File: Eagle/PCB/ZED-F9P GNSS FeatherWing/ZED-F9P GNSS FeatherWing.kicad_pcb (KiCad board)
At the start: 2 copper layers, 50.8 x 22.9 mm, 42 parts, among them Q1 DMG2305, U1 ZED-F9P_ZED-F9P, U2 SPX3819-3.3, X1 SMA-142-0711-821/826

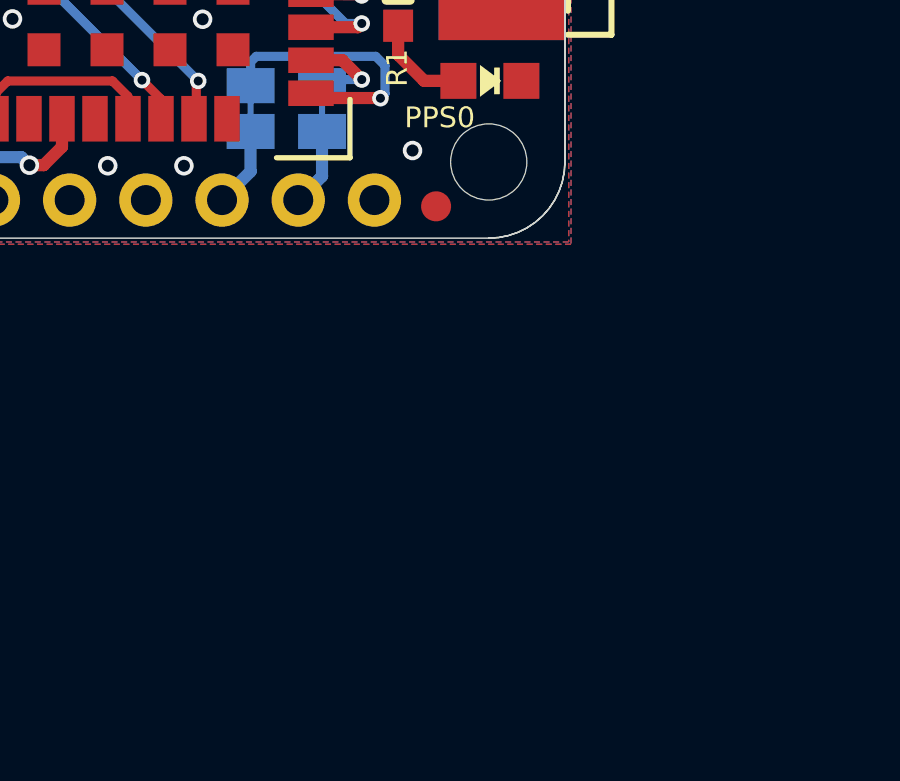
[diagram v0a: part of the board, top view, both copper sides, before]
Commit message: Update to Kicad 10 and added SMA
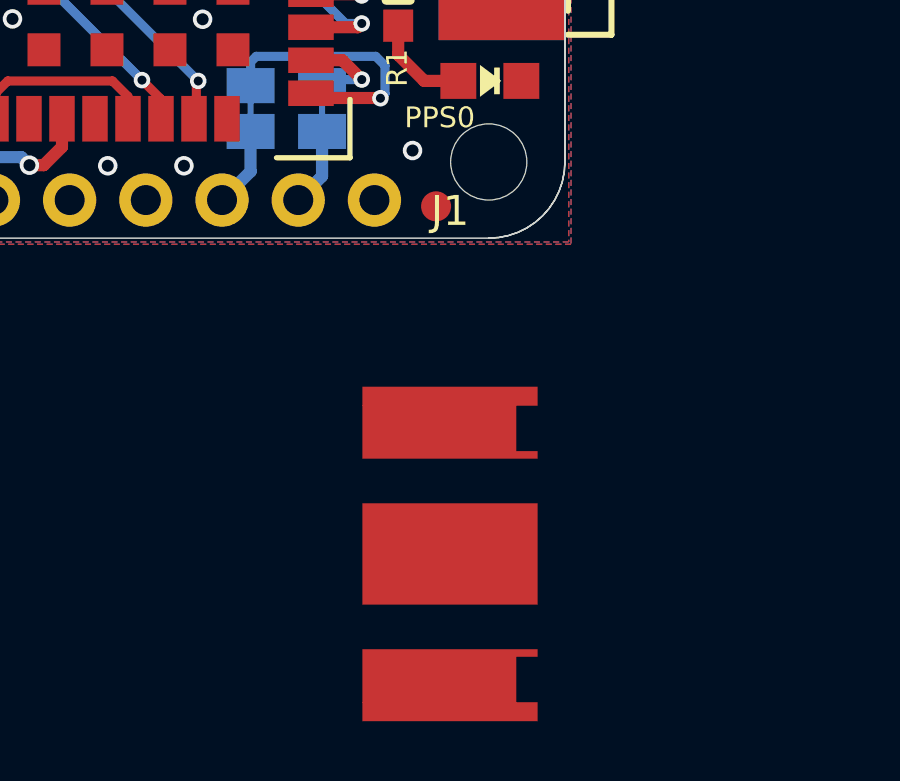
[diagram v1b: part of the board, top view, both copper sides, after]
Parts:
- added J1: Coupler_v2_Coupler_v2-rescue_SMA-Coupler_v1-rescue, Coupler_v1:SMA_Molex_732511150_v3, F.Cu at (170.1, 127.0)
- CON1: value (none) -> MICROBUILDER_USBFCI_10103594_CORRECTED
- CTS0, GND0, RTS0, RX2, TX2, UNK3V3: value (none) -> PINHD-1X1
- INT0, RX0, SCL0, SDA0, TX0: value (none) -> SOLDERJUMPERCLOSED
- JP5: value (none) -> HEADER-1X2ROUND
- TP1: value (none) -> TESTPOINTROUND1.5MM
- UNK3.3V0: value (none) -> SOLDERJUMPER
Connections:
- net 3V renamed Net-(MS1-3V)
- net ANT renamed /ANT
- net D+ renamed /D+
- net D- renamed /D-
- net EN renamed /EN
- net EXTINT renamed /EXTINT
- net RX renamed /RX
- net RX2 renamed /RX2
- net SAFEBOOT renamed /SAFEBOOT
- net SCL renamed /SCL
- net SDA renamed /SDA
- net TP renamed /TP
- net TX renamed /TX
- net TX2 renamed /TX2
- net VBACKUP renamed /VBACKUP
- net VCC_RF renamed /VCC_RF
- net ~{RESET} renamed /~{RESET}
- CON1 pad ID: (no net) -> unconnected-(CON1-PadID)
- CTS0 pad 1: (no net) -> unconnected-(CTS0-Pad1)
- MS1 pad 10: (no net) -> unconnected-(MS1-GPIOA5-Pad10)
- MS1 pad 11: (no net) -> unconnected-(MS1-GPIOSCK-Pad11)
- MS1 pad 12: (no net) -> unconnected-(MS1-GPIOMOSI-Pad12)
- MS1 pad 13: (no net) -> unconnected-(MS1-GPIOMISO-Pad13)
- MS1 pad 16: (no net) -> unconnected-(MS1-NC-Pad16)
- MS1 pad 19: (no net) -> unconnected-(MS1-GPIO5-Pad19)
- MS1 pad 20: (no net) -> unconnected-(MS1-GPIO6-Pad20)
- MS1 pad 21: (no net) -> unconnected-(MS1-GPIO9-Pad21)
- MS1 pad 22: (no net) -> unconnected-(MS1-GPIO10-Pad22)
- MS1 pad 23: (no net) -> unconnected-(MS1-GPIO11-Pad23)
- MS1 pad 24: (no net) -> unconnected-(MS1-GPIO12-Pad24)
- MS1 pad 25: (no net) -> unconnected-(MS1-GPIO13-Pad25)
- MS1 pad 3: (no net) -> unconnected-(MS1-AREF-Pad3)
- MS1 pad 5: (no net) -> unconnected-(MS1-GPIOA0-Pad5)
- MS1 pad 6: (no net) -> unconnected-(MS1-GPIOA1-Pad6)
- MS1 pad 8: (no net) -> unconnected-(MS1-GPIOA3-Pad8)
- MS1 pad 9: (no net) -> unconnected-(MS1-GPIOA4-Pad9)
- RTS0 pad 1: (no net) -> unconnected-(RTS0-Pad1)
- U1 pad 19: (no net) -> unconnected-(U1-GEO_STAT-Pad19)
- U1 pad 20: (no net) -> unconnected-(U1-RTK_STAT-Pad20)
- U1 pad 4: (no net) -> unconnected-(U1-ANT_DETECT-Pad4)
- U1 pad 46: (no net) -> unconnected-(U1-TX_READY-Pad46)
- U1 pad 47: (no net) -> unconnected-(U1-D_SEL-Pad47)
- U1 pad 5: (no net) -> unconnected-(U1-ANT_OFF-Pad5)
- U1 pad 6: (no net) -> unconnected-(U1-~{ANT_SHORT}-Pad6)
- U2 pad 4: (no net) -> unconnected-(U2-P4-Pad4)

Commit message: V2 Release
Released to fab.
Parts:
- removed X1: SMA-142-0711-821/826, ZED-F9P GNSS FeatherWing:J502-ND-142-0711-821_826_133
- added C5: C_Small_US, Capacitor_SMD:C_0402_1005Metric, F.Cu at (158.2, 113.8)
- added C6: C_Small_US, Capacitor_SMD:C_0402_1005Metric, F.Cu at (152.5, 113.8)
- added FID3: FIDUCIAL"", Fiducial:Fiducial_0.5mm_Mask1mm, F.Cu at (172.9, 97.8)
- C3: value 10nF -> 47pF; footprint ZED-F9P GNSS FeatherWing:0805-NO -> Capacitor_SMD:C_0402_1005Metric
- FID1, FID2: footprint ZED-F9P GNSS FeatherWing:FIDUCIAL_1MM -> Fiducial:Fiducial_0.5mm_Mask1mm
- INT0, RX0, SCL0, SDA0, TX0: footprint ZED-F9P GNSS FeatherWing:SOLDERJUMPER_CLOSEDWIRE -> Jumper:SolderJumper-2_P1.3mm_Bridged_RoundedPad1.0x1.5mm
- J1: value Coupler_v2_Coupler_v2-rescue_SMA-Coupler_v1-rescue -> EdgeMount_SMA; footprint Coupler_v1:SMA_Molex_732511150_v3 -> Coupler_v1:SMA_Molex_0732512120
- L1: value 27nH -> 100nH; footprint ZED-F9P GNSS FeatherWing:0805-NO -> Inductor_SMD:L_0603_1608Metric
- R2: footprint ZED-F9P GNSS FeatherWing:0805-NO -> Resistor_SMD:R_0402_1005Metric
- R6, R7: value 100K -> 10K
- U1: value ZED-F9P_ZED-F9P -> ZED-F9P-15B
- UNK3.3V0: footprint ZED-F9P GNSS FeatherWing:SOLDERJUMPER_ARROW_NOPASTE -> Jumper:SolderJumper-2_P1.3mm_Open_RoundedPad1.0x1.5mm
- moved J1 22.0 mm to (171.8, 105.0)
- moved C3 4.47 mm to (167.9, 101.2), turned to 180 degrees
- moved C4 4.15 mm to (127.1, 112.2), turned to 135 degrees
- moved C2 2.82 mm to (139.0, 112.0), turned to -90 degrees
- moved Z3 1.84 mm to (131.3, 101.7)
- moved Z1 1.82 mm to (131.3, 100.4)
- moved C1 1.73 mm to (141.0, 112.0), turned to -90 degrees
- moved L1 1.63 mm to (168.6, 104.2)
- moved R2 1.54 mm to (167.8, 97.4), turned to 180 degrees
- moved Q1 0.98 mm to (137.7, 103.3), turned to 0 degrees
- moved Z4 0.84 mm to (134.7, 101.7)
- moved Z2 0.79 mm to (134.7, 100.4)
- moved PPS0 0.36 mm to (171.4, 111.5)
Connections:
- J1 pad 1: unconnected-(J1-Signal-Pad1) -> /ANT
- J1 pad 2: unconnected-(J1-GND-Pad2) -> GND
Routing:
- net GND: track 156.3 -> 24.6 mm, vias 41 -> 180
- net 3.3V: track 75.0 -> 17.9 mm, vias 2 -> 9
- net VBUS: track 36.5 -> 7.16 mm, vias 2 -> 7
- net /TP: track 11.8 -> 20.7 mm
- net Net-(MS1-GPIOSDA): track 26.4 -> 31.6 mm, vias 0 -> 1
- net /ANT: track 17.8 -> 22.7 mm
- net Net-(MS1-GPIOSCL): track 26.2 -> 30.8 mm, vias 0 -> 1
- net /EXTINT: track 32.3 -> 35.4 mm
- net /D-: track 42.1 -> 45.2 mm
- net /VBACKUP: track 37.4 -> 40.4 mm
- net /SAFEBOOT: track 3.35 -> 6.09 mm
- net Net-(Q1-S): track 22.9 -> 20.3 mm
- net VBAT: track 11.1 -> 9.18 mm
- net Net-(L1-P$1): track 4.71 -> 6.22 mm
- net /EN: track 21.1 -> 22.4 mm
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- added copper zone on In1.Cu, net 3.3V
- added copper zone on In1.Cu, net GND
- added copper zone on In2.Cu, net GND
- added copper zone on In1.Cu, net VBUS
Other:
- copper layers 2 -> 4
- board text added: "github.com/laberge1/ZED-F9P_FeatherWing_USB"
- board text removed: "3V3"
- board text removed: "FeatherWing"
